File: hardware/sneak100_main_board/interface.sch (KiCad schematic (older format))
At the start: 19 parts, among them J11 Conn_01x06, SW2 SW_Push, SW3 SW_Push, SW4 SW_Push, U10 SSD1306, U11 TSOP4838

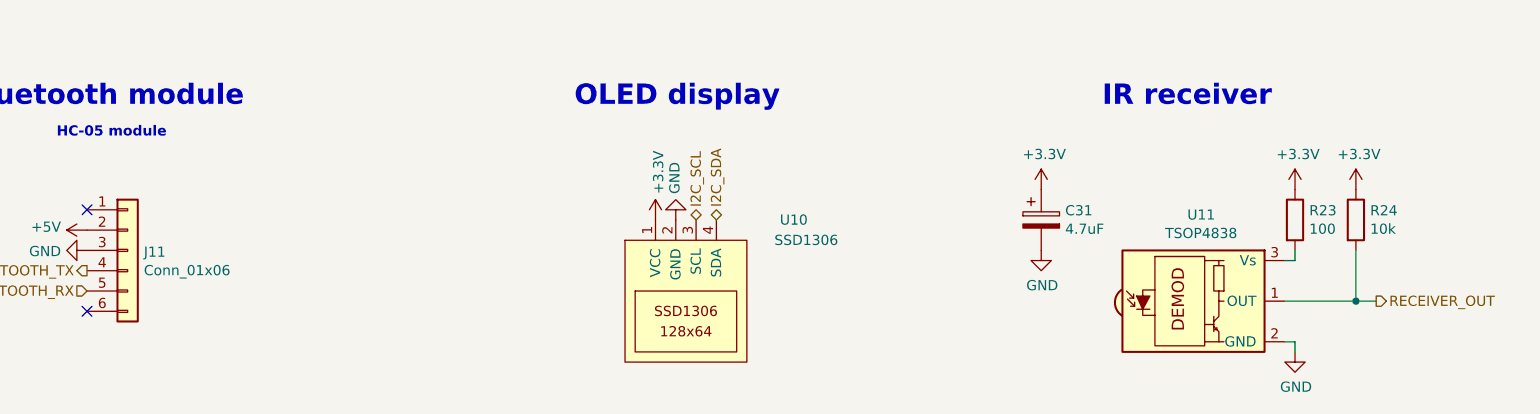
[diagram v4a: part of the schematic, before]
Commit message: More space in top hull and schematic fix
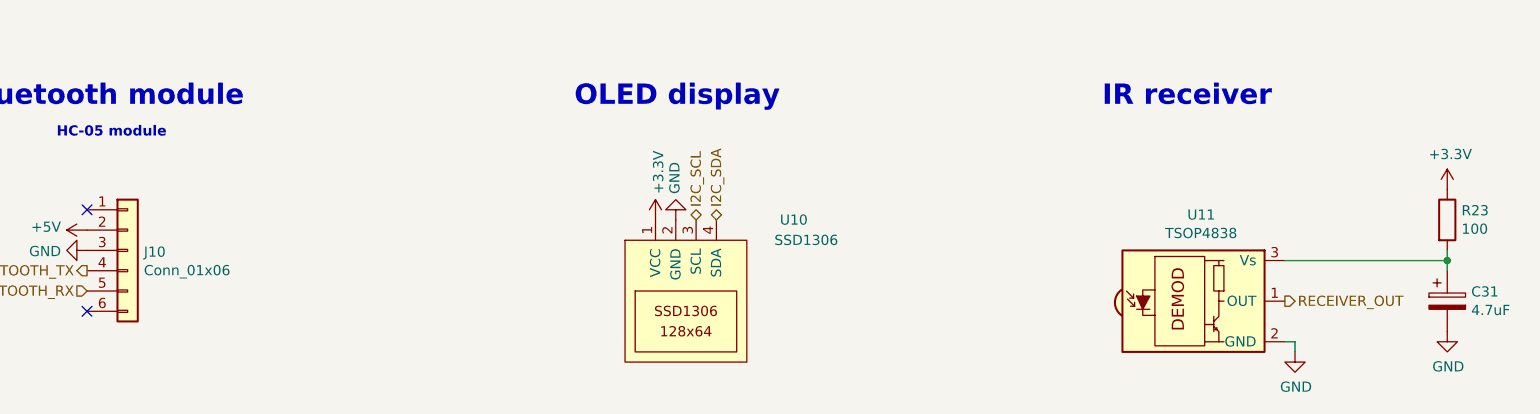
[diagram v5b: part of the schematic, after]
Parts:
- removed R24: 10k, Resistor_SMD:R_0603_1608Metric, symbol Device:R
- renumbered J11 to J10
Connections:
- net +3V3: no longer C31.1
- net at R23.2, U11.3 (Vs): now also C31.1
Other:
- moved on the sheet: C31, R23
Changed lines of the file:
@@
 bluetooth module
 $Comp
-L Connector_Generic:Conn_01x06 J11
+L Connector_Generic:Conn_01x06 J10
 U 1 1 60F1EA00
 P 3350 4450
-F 0 "J11" H 3430 4442 50  0000 L CNN
+F 0 "J10" H 3430 4442 50  0000 L CNN
 F 1 "Conn_01x06" H 3430 4351 50  0000 L CNN
 F 2 "Connector_PinSocket_2.54mm:PinSocket_1x06_P2.54mm_Vertical" H 3350 4450 50  0001 C CNN
@@
 BLUETOOTH_TX
 $Comp
-L power:GND #PWR0127
+L power:GND #PWR0126
 U 1 1 60F1FEEB
 P 3150 4450
-F 0 "#PWR0127" H 3150 4200 50  0001 C CNN
+F 0 "#PWR0126" H 3150 4200 50  0001 C CNN
 F 1 "GND" V 3155 4322 50  0000 R CNN
 F 2 "" H 3150 4450 50  0001 C CNN
@@
 $EndComp
 $Comp
-L power:+5V #PWR0126
+L power:+5V #PWR0125
 U 1 1 60F200B0
 P 3150 4350
-F 0 "#PWR0126" H 3150 4200 50  0001 C CNN
+F 0 "#PWR0125" H 3150 4200 50  0001 C CNN
 F 1 "+5V" V 3165 4478 50  0000 L CNN
 F 2 "" H 3150 4350 50  0001 C CNN
@@
 $EndComp
 $Comp
-L power:GND #PWR0129
+L power:GND #PWR0128
 U 1 1 60F7CCD5
 P 9100 4950
-F 0 "#PWR0129" H 9100 4700 50  0001 C CNN
+F 0 "#PWR0128" H 9100 4700 50  0001 C CNN
 F 1 "GND" H 9105 4777 50  0000 C CNN
 F 2 "" H 9100 4950 50  0001 C CNN
@@
 $EndComp
 $Comp
-L power:+3.3V #PWR0123
-U 1 1 60F7DC2F
-P 9400 4150
-F 0 "#PWR0123" H 9400 4000 50  0001 C CNN
-F 1 "+3.3V" H 9415 4323 50  0000 C CNN
-F 2 "" H 9400 4150 50  0001 C CNN
-F 3 "" H 9400 4150 50  0001 C CNN
-	1    9400 4150
-	1    0    0    -1
-$EndComp
-$Comp
 L Device:CP C31
 U 1 1 60F7F945
-P 7850 4300
-F 0 "C31" H 7968 4346 50  0000 L CNN
-F 1 "4.7uF" H 7968 4255 50  0000 L CNN
-F 2 "Capacitor_THT:CP_Radial_D5.0mm_P2.00mm" H 7888 4150 50  0001 C CNN
-F 3 "~" H 7850 4300 50  0001 C CNN
-	1    7850 4300
-	1    0    0    -1
-$EndComp
-$Comp
-L power:GND #PWR0128
+P 9850 4700
+F 0 "C31" H 9968 4746 50  0000 L CNN
+F 1 "4.7uF" H 9968 4655 50  0000 L CNN
+F 2 "Capacitor_THT:CP_Radial_D5.0mm_P2.00mm" H 9888 4550 50  0001 C CNN
+F 3 "~" H 9850 4700 50  0001 C CNN
+	1    9850 4700
+	1    0    0    -1
+$EndComp
+$Comp
+L power:GND #PWR0127
 U 1 1 60F80FC7
-P 7850 4450
-F 0 "#PWR0128" H 7850 4200 50  0001 C CNN
-F 1 "GND" H 7855 4277 50  0000 C CNN
-F 2 "" H 7850 4450 50  0001 C CNN
-F 3 "" H 7850 4450 50  0001 C CNN
-	1    7850 4450
-	1    0    0    -1
-$EndComp
-$Comp
-L power:+3.3V #PWR0121
-U 1 1 60F81378
-P 7850 4150
-F 0 "#PWR0121" H 7850 4000 50  0001 C CNN
-F 1 "+3.3V" H 7865 4323 50  0000 C CNN
-F 2 "" H 7850 4150 50  0001 C CNN
-F 3 "" H 7850 4150 50  0001 C CNN
-	1    7850 4150
+P 9850 4850
+F 0 "#PWR0127" H 9850 4600 50  0001 C CNN
+F 1 "GND" H 9855 4677 50  0000 C CNN
+F 2 "" H 9850 4850 50  0001 C CNN
+F 3 "" H 9850 4850 50  0001 C CNN
+	1    9850 4850
 	1    0    0    -1
 $EndComp
@@
 L Device:R R23
 U 1 1 60F8B46D
-P 9100 4300
-F 0 "R23" H 9170 4346 50  0000 L CNN
-F 1 "100" H 9170 4255 50  0000 L CNN
-F 2 "Resistor_SMD:R_0603_1608Metric" V 9030 4300 50  0001 C CNN
-F 3 "~" H 9100 4300 50  0001 C CNN
-	1    9100 4300
+P 9850 4300
+F 0 "R23" H 9920 4346 50  0000 L CNN
+F 1 "100" H 9920 4255 50  0000 L CNN
+F 2 "Resistor_SMD:R_0603_1608Metric" V 9780 4300 50  0001 C CNN
+F 3 "~" H 9850 4300 50  0001 C CNN
+	1    9850 4300
 	1    0    0    -1
 $EndComp
@@
 L power:+3.3V #PWR0122
 U 1 1 60F8BCE9
-P 9100 4150
-F 0 "#PWR0122" H 9100 4000 50  0001 C CNN
-F 1 "+3.3V" H 9115 4323 50  0000 C CNN
-F 2 "" H 9100 4150 50  0001 C CNN
-F 3 "" H 9100 4150 50  0001 C CNN
-	1    9100 4150
-	1    0    0    -1
-$EndComp
-Wire Wire Line
-	9050 4500 9100 4500
-Wire Wire Line
-	9100 4500 9100 4450
+P 9850 4150
+F 0 "#PWR0122" H 9850 4000 50  0001 C CNN
+F 1 "+3.3V" H 9865 4323 50  0000 C CNN
+F 2 "" H 9850 4150 50  0001 C CNN
+F 3 "" H 9850 4150 50  0001 C CNN
+	1    9850 4150
+	1    0    0    -1
+$EndComp
 Wire Wire Line
 	9050 4900 9100 4900
 Wire Wire Line
 	9100 4900 9100 4950
-$Comp
-L Device:R R24
-U 1 1 60F9B98E
-P 9400 4300
-F 0 "R24" H 9470 4346 50  0000 L CNN
-F 1 "10k" H 9470 4255 50  0000 L CNN
-F 2 "Resistor_SMD:R_0603_1608Metric" V 9330 4300 50  0001 C CNN
-F 3 "~" H 9400 4300 50  0001 C CNN
-	1    9400 4300
-	1    0    0    -1
-$EndComp
-Wire Wire Line
-	9050 4700 9400 4700
-Wire Wire Line
-	9400 4700 9400 4450
-Wire Wire Line
-	9400 4700 9500 4700
-Connection ~ 9400 4700
-Text HLabel 9500 4700 2    50   Output ~ 0
+Text HLabel 9050 4700 2    50   Output ~ 0
 RECEIVER_OUT
 $Comp
@@
 BUTTON_R
 $Comp
-L power:+3.3V #PWR0124
+L power:+3.3V #PWR0123
 U 1 1 60FBF32E
 P 5950 4300
-F 0 "#PWR0124" H 5950 4150 50  0001 C CNN
+F 0 "#PWR0123" H 5950 4150 50  0001 C CNN
 F 1 "+3.3V" V 5965 4428 50  0000 L CNN
 F 2 "" H 5950 4300 50  0001 C CNN
@@
 $EndComp
 $Comp
-L power:GND #PWR0125
+L power:GND #PWR0124
 U 1 1 60FBFC20
 P 6050 4300
-F 0 "#PWR0125" H 6050 4050 50  0001 C CNN
+F 0 "#PWR0124" H 6050 4050 50  0001 C CNN
 F 1 "GND" V 6055 4172 50  0000 R CNN
 F 2 "" H 6050 4300 50  0001 C CNN
@@
 	1    0    0    -1
 $EndComp
+Wire Wire Line
+	9850 4450 9850 4500
+Wire Wire Line
+	9050 4500 9850 4500
+Connection ~ 9850 4500
+Wire Wire Line
+	9850 4500 9850 4550
 $EndSCHEMATC

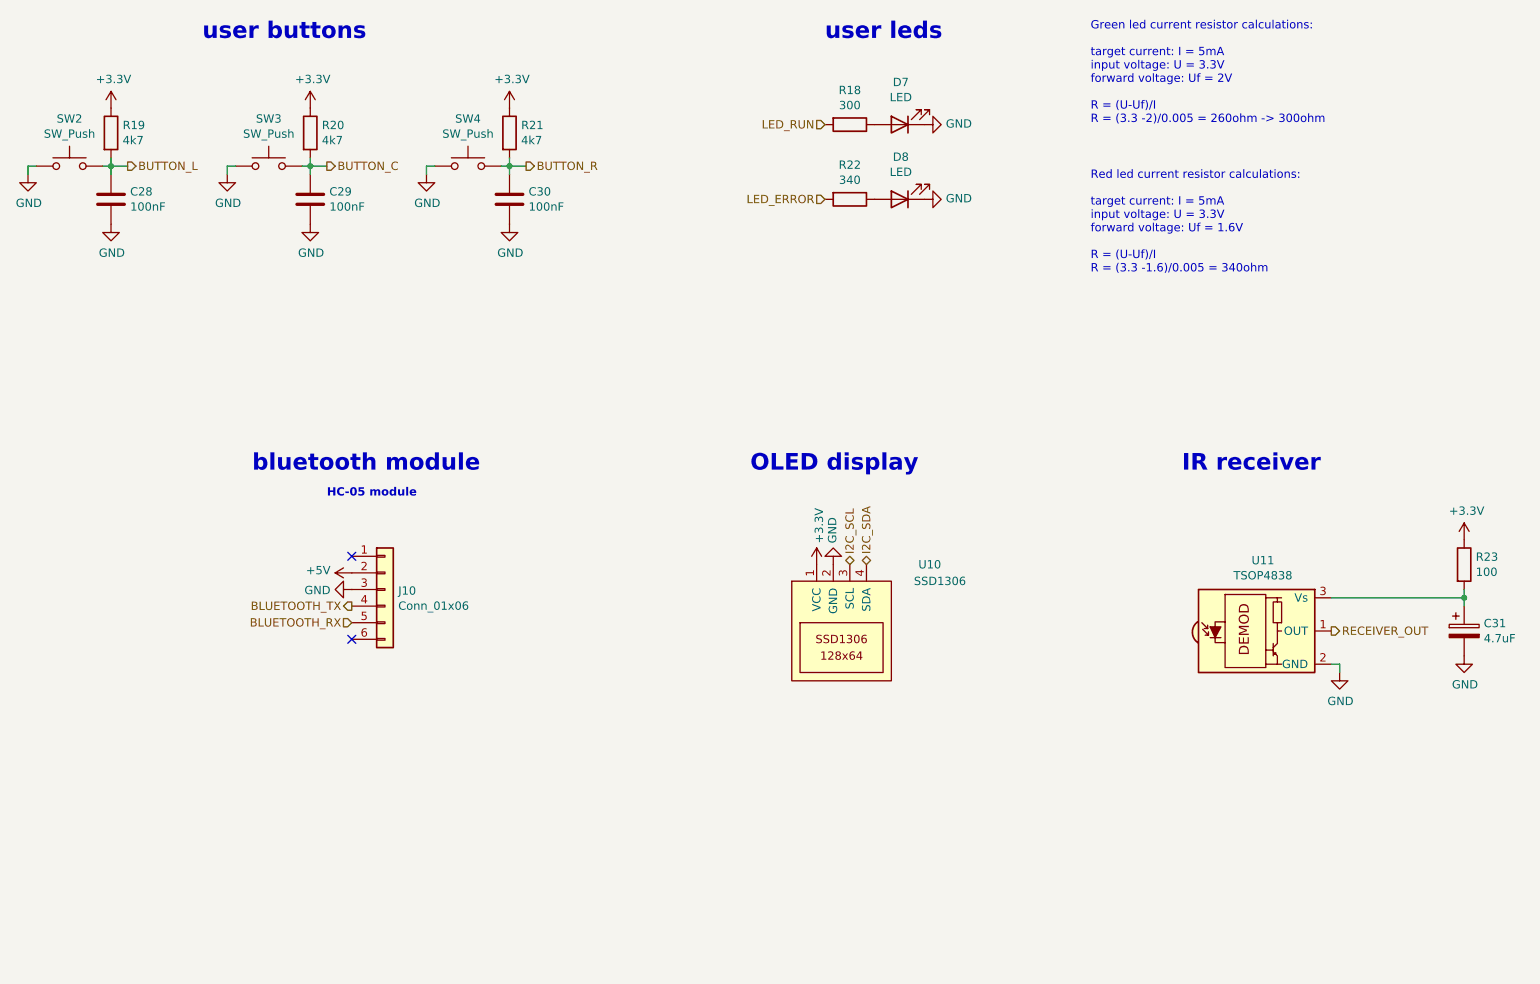
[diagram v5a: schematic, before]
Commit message: bluetooth en & status connection
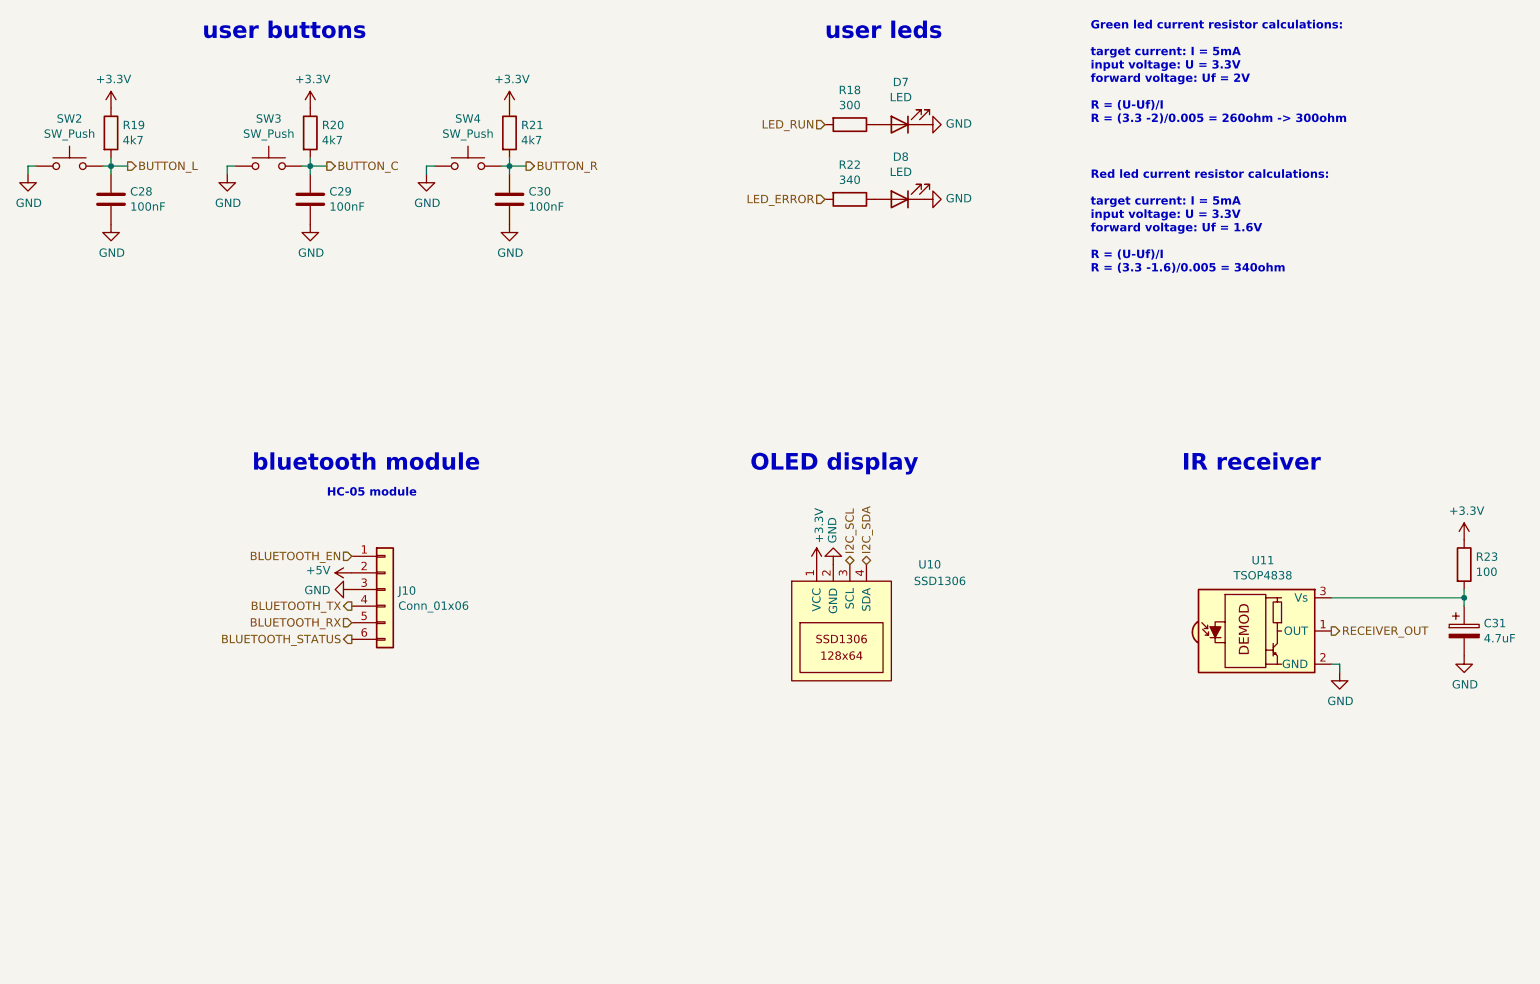
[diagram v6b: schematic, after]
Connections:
- net BLUETOOTH_EN: now reaches J10.1 (Pin_1)
- net BLUETOOTH_STATUS: now reaches J10.6 (Pin_6)
- no-connect marks 2 -> 0
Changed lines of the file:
@@
 Text HLabel 6000 1650 0    50   Input ~ 0
 LED_RUN
-Text Notes 7600 1650 0    50   ~ 0
+Text Notes 7600 1650 0    50   ~ 10
 Green led current resistor calculations:\n\ntarget current: I = 5mA\ninput voltage: U = 3.3V\nforward voltage: Uf = 2V\n\nR = (U-Uf)/I\nR = (3.3 -2)/0.005 = 260ohm -> 300ohm
 Text Notes 2250 1150 0    100  ~ 20
@@
 	1    0    0    -1
 $EndComp
-NoConn ~ 3150 4250
-NoConn ~ 3150 4750
 Text HLabel 3150 4650 0    50   Input ~ 0
 BLUETOOTH_RX
@@
 Text HLabel 6000 2100 0    50   Input ~ 0
 LED_ERROR
-Text Notes 7600 2550 0    50   ~ 0
+Text Notes 7600 2550 0    50   ~ 10
 Red led current resistor calculations:\n\ntarget current: I = 5mA\ninput voltage: U = 3.3V\nforward voltage: Uf = 1.6V\n\nR = (U-Uf)/I\nR = (3.3 -1.6)/0.005 = 340ohm
 Text Notes 3000 3900 0    50   ~ 10
@@
 Wire Wire Line
 	9850 4500 9850 4550
+Text HLabel 3150 4250 0    50   Input ~ 0
+BLUETOOTH_EN
+Text HLabel 3150 4750 0    50   Output ~ 0
+BLUETOOTH_STATUS
 $EndSCHEMATC
